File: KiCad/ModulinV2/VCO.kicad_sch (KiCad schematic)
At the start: 99 parts, among them Q1 MMBFJ201, Q2 MMBFJ201, SW3 SW_SPDT_MSM, U3 AS3340, U4 AS3340, U5 TL074HIDR, U6 TL074HIDR, U7 TL072HIDR

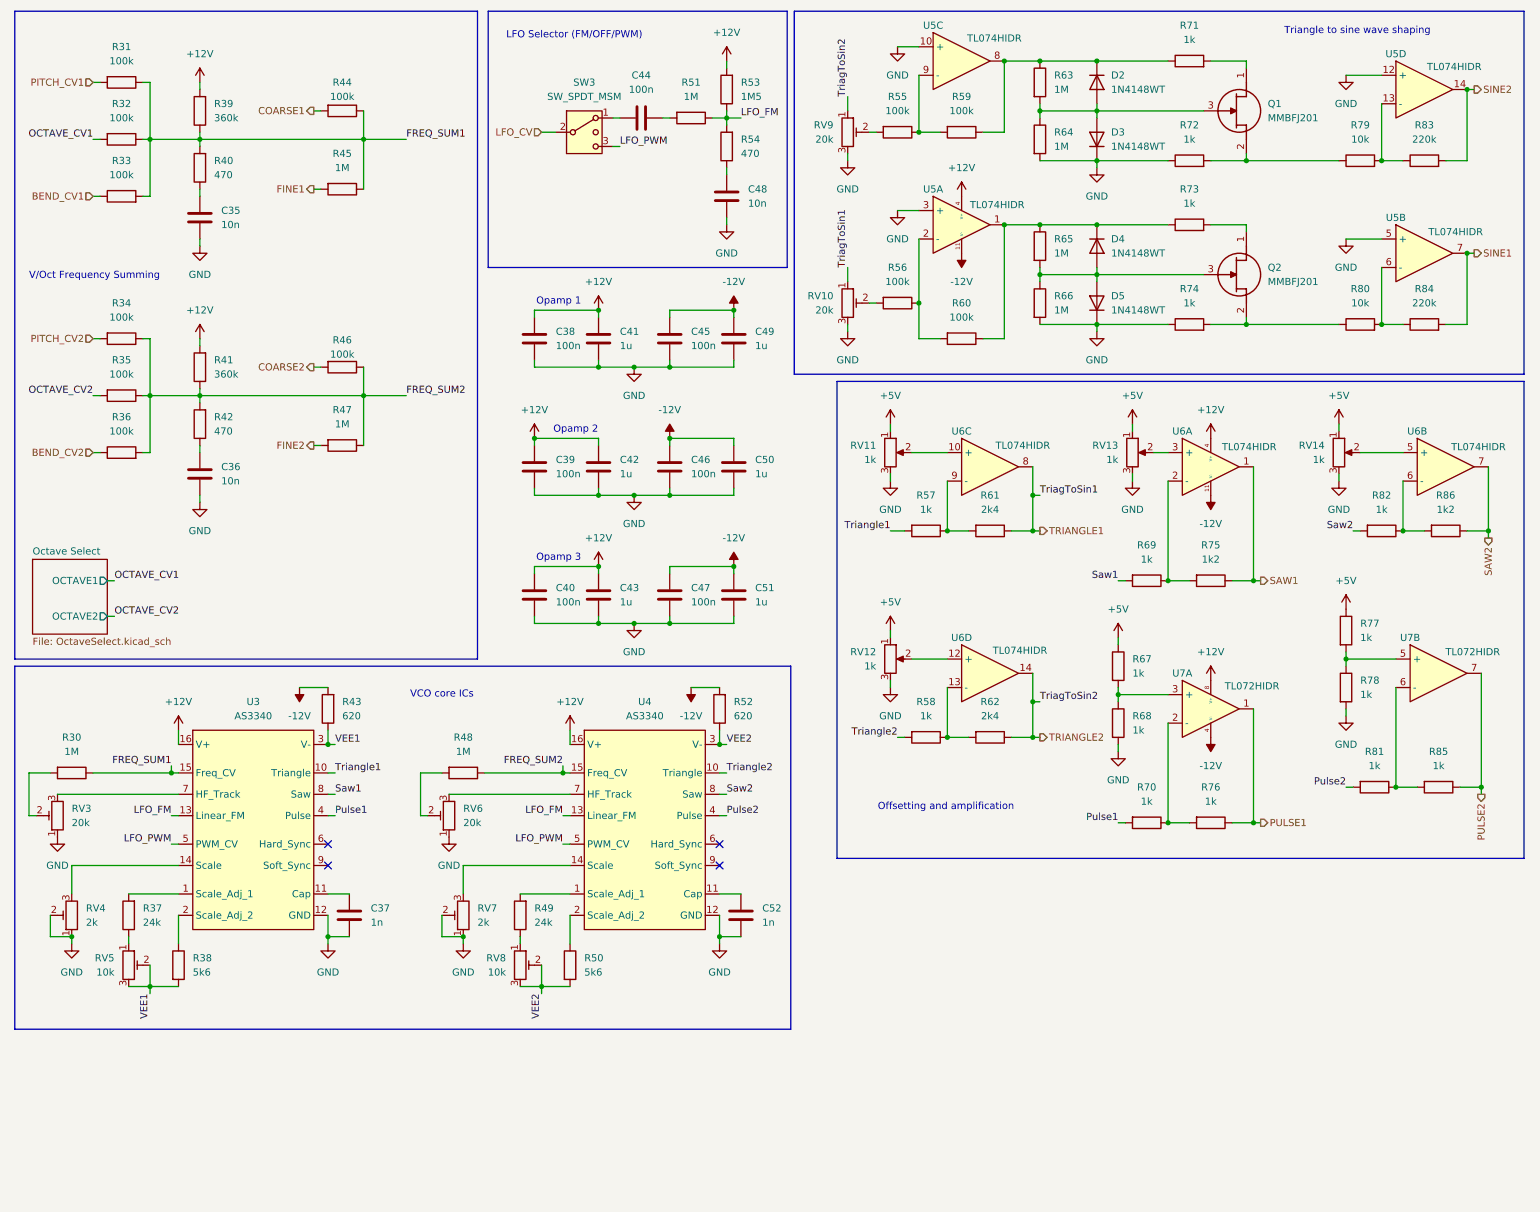
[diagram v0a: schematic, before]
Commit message: Fixed library issues and assigned most footprints
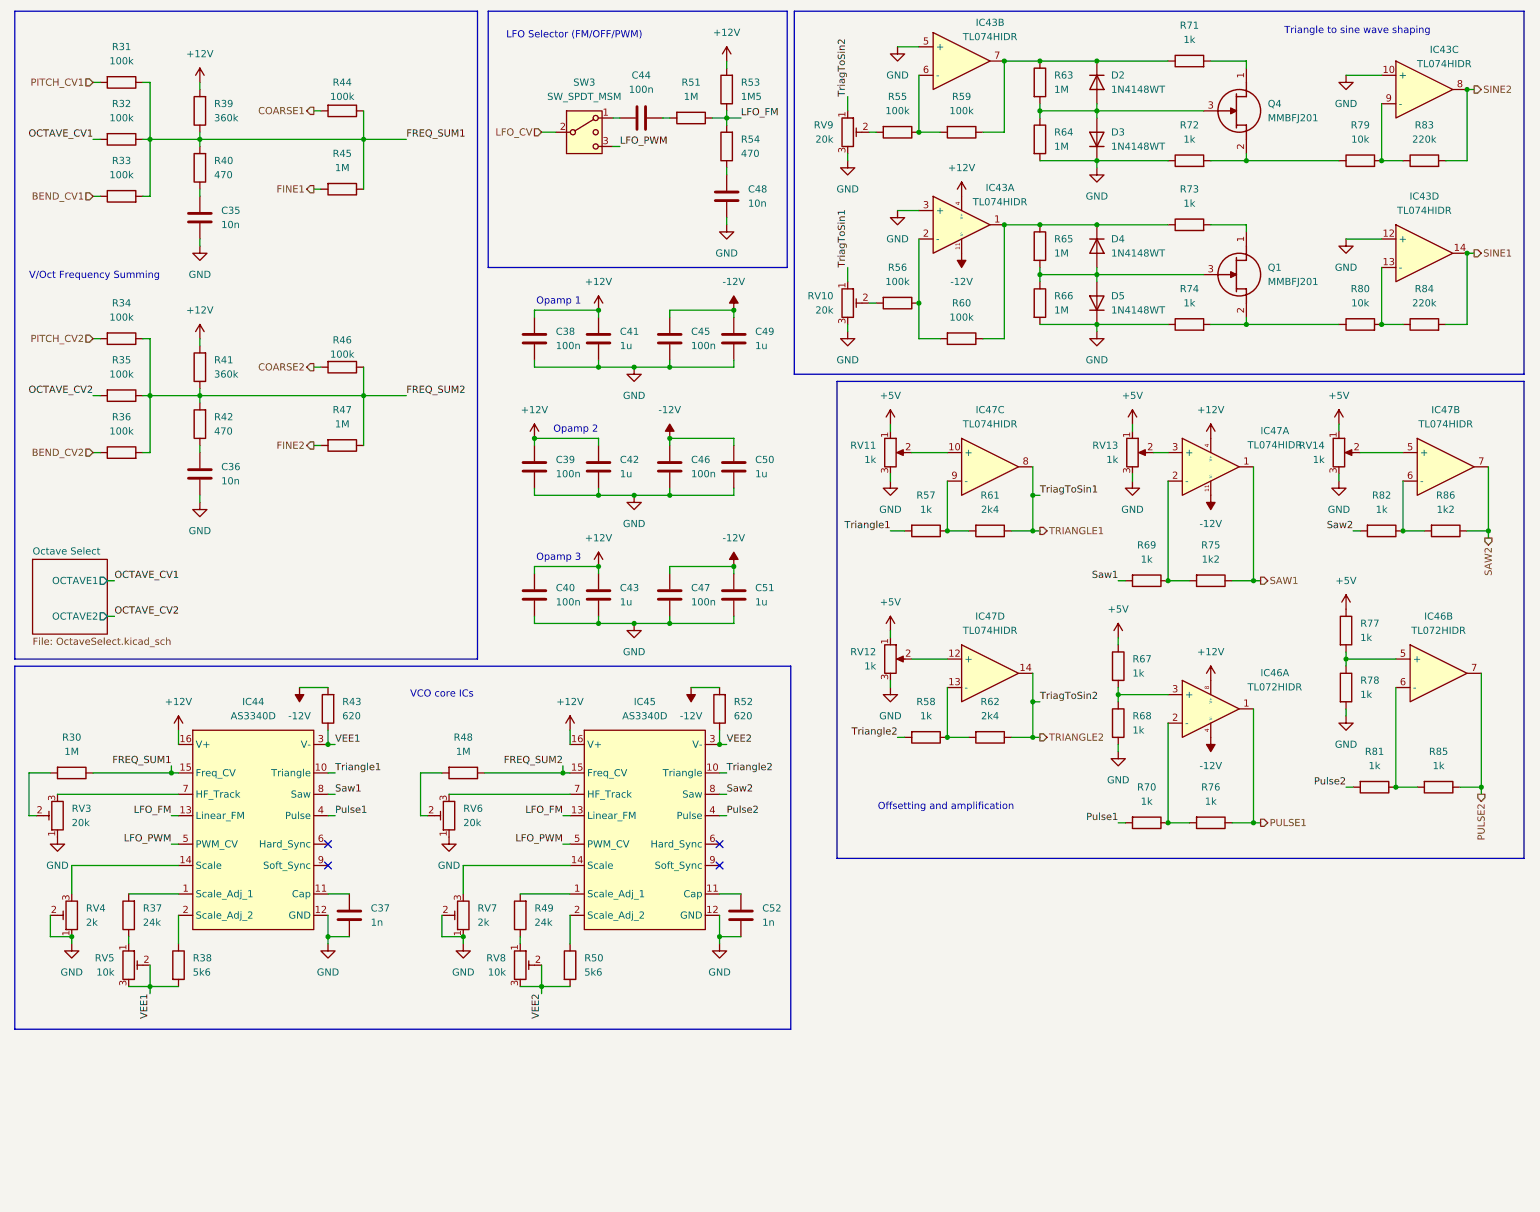
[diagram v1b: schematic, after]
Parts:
- removed Q1, Q2: MMBFJ201, SOT95P240X120-3N, symbol MMBFJ201:MMBFJ201
- removed U3, U4: AS3340, symbol AS3340:AS3340
- removed U5, U6: TL074HIDR, symbol TL074HIDR:TL074HIDRx4
- removed U7: TL072HIDR, symbol TL072HIDR:TL072HIDRx2
- added IC43, IC47: TL074HIDR, SamacSys_Parts:SOIC127P600X175-14N, symbol SamacSys_Parts:TL074HIDR
- added IC44, IC45: AS3340D, SamacSys_Parts:DIP762W46P254L2007H436Q16N, symbol SamacSys_Parts:AS3340D
- added IC46: TL072HIDR, SamacSys_Parts:SOIC127P600X175-8N, symbol SamacSys_Parts:TL072HIDR
- added Q1, Q4: MMBFJ201, SamacSys_Parts:SOT95P240X120-3N, symbol SamacSys_Parts:MMBFJ201
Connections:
- net +12V: now also IC43.4 (V+), IC44.16 (V+), IC45.16 (V+), IC46.8 (V+), IC47.4 (V+)
- net -12V: now also IC43.11 (V-), IC46.4 (V-), IC47.11 (V-)
- net FREQ_SUM1: now also IC44.15 (Freq_CV)
- net FREQ_SUM2: now also IC45.15 (Freq_CV)
- net GND: now also IC43.10 (+), IC43.12 (+), IC43.3 (+), IC43.5 (+), IC44.12 (GND), IC45.12 (GND)
- net LFO_FM: now also IC44.13 (Linear_FM), IC45.13 (Linear_FM)
- net LFO_PWM: now also IC44.5 (PWM_CV), IC45.5 (PWM_CV)
- net PULSE1: now also IC46.1
- net PULSE2: now also IC46.7
- net Pulse1: now also IC44.4 (Pulse)
- net Pulse2: now also IC45.4 (Pulse)
- net SAW1: now also IC47.1
- net SAW2: now also IC47.7
- net SINE1: now also IC43.14
- net SINE2: now also IC43.8
- net Saw1: now also IC44.8 (Saw)
- net Saw2: now also IC45.8 (Saw)
- net TRIANGLE1: now also IC47.8
- net TRIANGLE2: now also IC47.14
- net Triangle1: now also IC44.10 (Triangle)
- net Triangle2: now also IC45.10 (Triangle)
- net VEE1: now also IC44.3 (V-)
- net VEE2: now also IC45.3 (V-)
- net at RV14.2: now also IC47.5 (+)
- net at R82.1, R86.2: now also IC47.6 (-)
- net at R71.2: now also Q4.1 (D)
- net at R72.2, R79.1: now also Q4.2 (S)
- net at D2.2 (A), D3.2 (A), R63.2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: now also Q4.3 (G)
- net at D2.1 (K), R59.1, R63.1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: now also IC43.7
- net at C37.1: now also IC44.11 (Cap)
- net at R70.1, R76.2: now also IC46.2 (-)
- net at R67.2, R68.1: now also IC46.3 (+)
- net at RV11.2: now also IC47.10 (+)
- net at R57.1, R61.2: now also IC47.9 (-)
- net at D4.1 (K), R60.1, R65.1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: now also IC43.1
- net at R56.1, R60.2: now also IC43.2 (-)
- net at R79.2, R83.1: now also IC43.9 (-)
- net at R81.1, R85.2: now also IC46.6 (-)
- net at R37.2: now also IC44.1 (Scale_Adj_1)
- net at D4.2 (A), D5.2 (A), R65.2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: now also Q1.3 (G)
- net at RV3.3: now also IC44.7 (HF_Track)
- net at RV6.3: now also IC45.7 (HF_Track)
- net at R49.2: now also IC45.1 (Scale_Adj_1)
- net at C52.1: now also IC45.11 (Cap)
- net at RV7.3: now also IC45.14 (Scale)
- net at R50.1: now also IC45.2 (Scale_Adj_2)
- net at RV12.2: now also IC47.12 (+)
- net at R58.1, R62.2: now also IC47.13 (-)
- net at RV4.3: now also IC44.14 (Scale)
- net at R77.2, R78.1: now also IC46.5 (+)
- net at R74.2, R80.1: now also Q1.2 (S)
- net at R80.2, R84.1: now also IC43.13 (-)
- net at R38.1: now also IC44.2 (Scale_Adj_2)
- net at R69.1, R75.2: now also IC47.2 (-)
- net at RV13.2: now also IC47.3 (+)
- net at R55.1, R59.2: now also IC43.6 (-)
- net at R73.2: now also Q1.1 (D)

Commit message: Changed switch for the boot and nrst. Fixed the GATE interface trigger
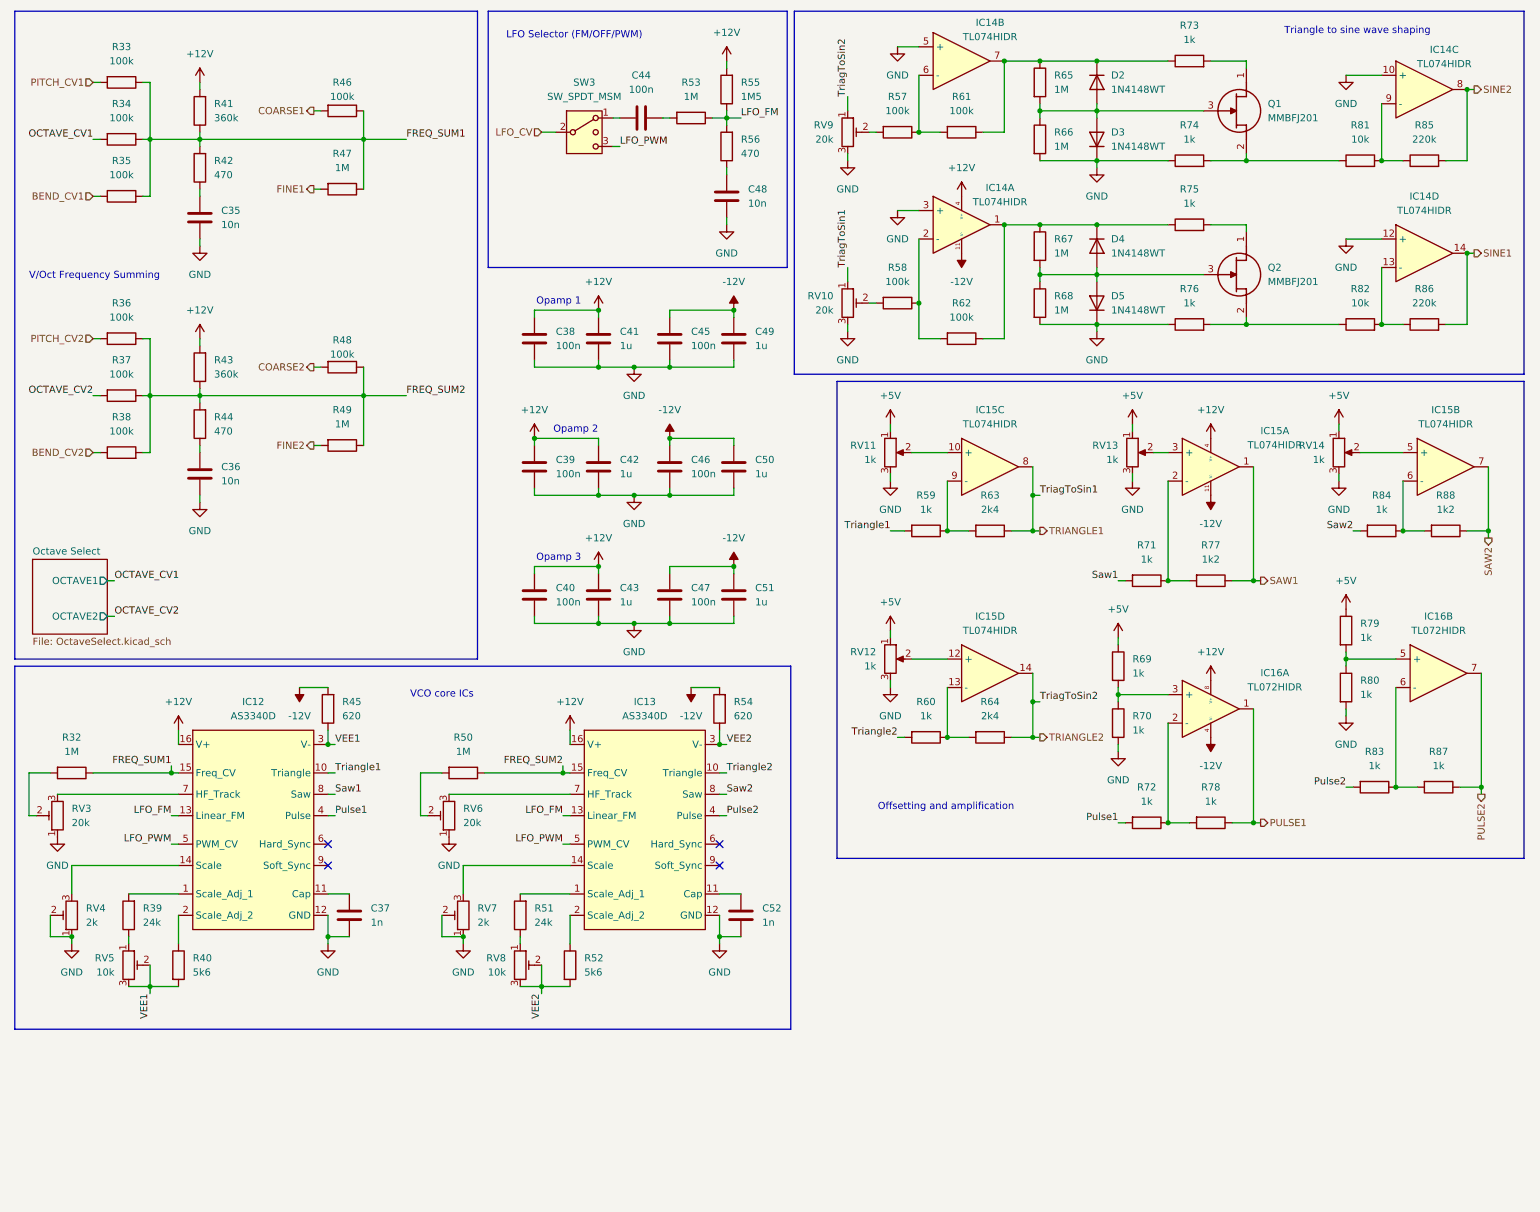
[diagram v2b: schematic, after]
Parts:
- renumbered IC44 to IC12, IC45 to IC13, IC43 to IC14, IC47 to IC15, IC46 to IC16, Q4 to Q1, Q1 to Q2, R30 to R32, R31 to R33, R32 to R34, R33 to R35, R34 to R36, R35 to R37, R36 to R38, R37 to R39, R38 to R40, R39 to R41, R40 to R42, R41 to R43, R42 to R44, R43 to R45, R44 to R46, R45 to R47, R46 to R48, R47 to R49, R48 to R50, R49 to R51, R50 to R52, R51 to R53, R52 to R54, R53 to R55, R54 to R56, R55 to R57, R56 to R58, R57 to R59, R58 to R60, R59 to R61, R60 to R62, R61 to R63, R62 to R64, R63 to R65, R64 to R66, R65 to R67, R66 to R68, R67 to R69, R68 to R70, R69 to R71, R70 to R72, R71 to R73, R72 to R74, R73 to R75, R74 to R76, R75 to R77, R76 to R78, R77 to R79, R78 to R80, R79 to R81, R80 to R82, R81 to R83, R82 to R84, R83 to R85, R84 to R86, R85 to R87, R86 to R88

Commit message: Started adding footprints for capacitors
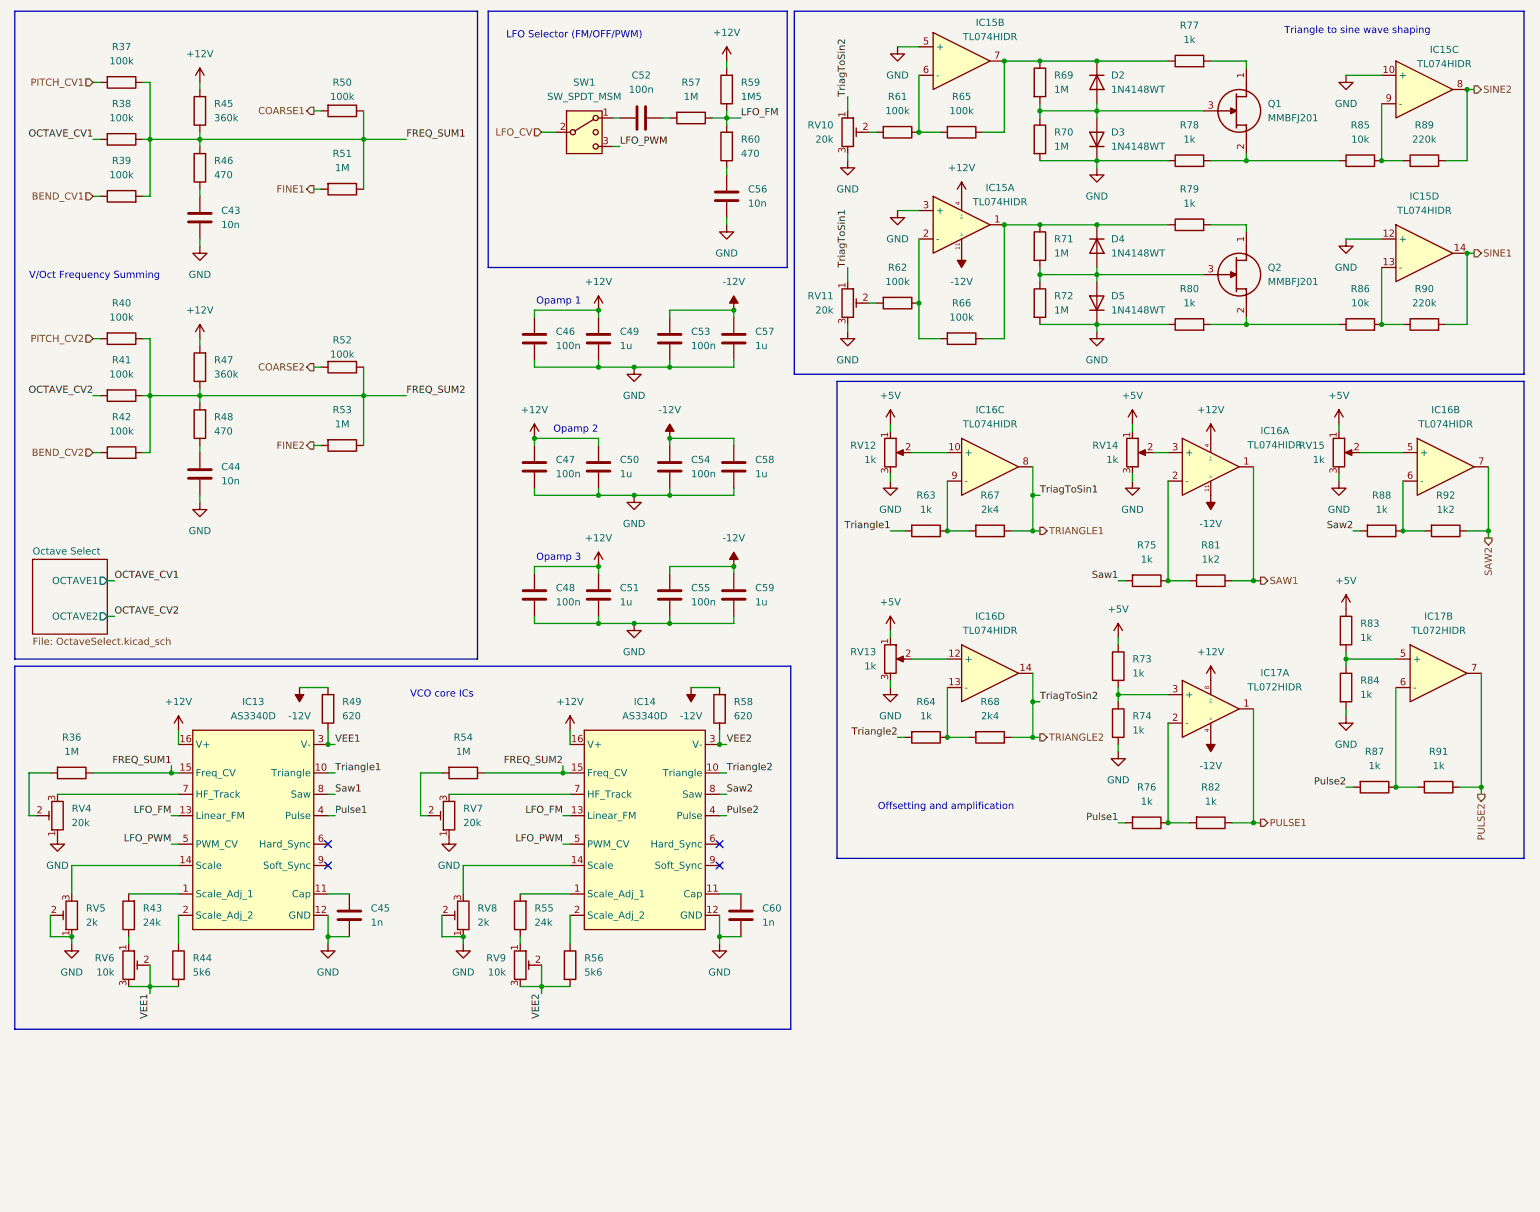
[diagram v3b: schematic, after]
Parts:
- C43: renamed from C35; footprint (none) -> SamacSys_Parts:CAPC1608X90N
- C44: renamed from C36; footprint (none) -> SamacSys_Parts:CAPC1608X90N
- C45: renamed from C37; footprint (none) -> SamacSys_Parts:CAPC1608X95N
- C46: renamed from C38; footprint (none) -> SamacSys_Parts:CAPC1608X90N
- C47: renamed from C39; footprint (none) -> SamacSys_Parts:CAPC1608X90N
- C48: renamed from C40; footprint (none) -> SamacSys_Parts:CAPC1608X90N
- C49: renamed from C41; footprint (none) -> SamacSys_Parts:CAPC1608X95N
- C50: renamed from C42; footprint (none) -> SamacSys_Parts:CAPC1608X95N
- C51: renamed from C43; footprint (none) -> SamacSys_Parts:CAPC1608X95N
- C52: renamed from C44; footprint (none) -> SamacSys_Parts:CAPC1608X90N
- C53: renamed from C45; footprint (none) -> SamacSys_Parts:CAPC1608X90N
- C54: renamed from C46; footprint (none) -> SamacSys_Parts:CAPC1608X90N
- C55: renamed from C47; footprint (none) -> SamacSys_Parts:CAPC1608X90N
- C56: renamed from C48; footprint (none) -> SamacSys_Parts:CAPC1608X90N
- C57: renamed from C49; footprint (none) -> SamacSys_Parts:CAPC1608X95N
- C58: renamed from C50; footprint (none) -> SamacSys_Parts:CAPC1608X95N
- C59: renamed from C51; footprint (none) -> SamacSys_Parts:CAPC1608X95N
- C60: renamed from C52; footprint (none) -> SamacSys_Parts:CAPC1608X95N
- SW1: renamed from SW3; footprint (none) -> SamacSys_Parts:SPDT
- renumbered IC12 to IC13, IC13 to IC14, IC14 to IC15, IC15 to IC16, IC16 to IC17, R32 to R36, R33 to R37, R34 to R38, R35 to R39, R36 to R40, R37 to R41, R38 to R42, R39 to R43, R40 to R44, R41 to R45, R42 to R46, R43 to R47, R44 to R48, R45 to R49, R46 to R50, R47 to R51, R48 to R52, R49 to R53, R50 to R54, R51 to R55, R52 to R56, R53 to R57, R54 to R58, R55 to R59, R56 to R60, R57 to R61, R58 to R62, R59 to R63, R60 to R64, R61 to R65, R62 to R66, R63 to R67, R64 to R68, R65 to R69, R66 to R70, R67 to R71, R68 to R72, R69 to R73, R70 to R74, R71 to R75, R72 to R76, R73 to R77, R74 to R78, R75 to R79, R76 to R80, R77 to R81, R78 to R82, R79 to R83, R80 to R84, R81 to R85, R82 to R86, R83 to R87, R84 to R88, R85 to R89, R86 to R90, R87 to R91, R88 to R92, RV9 to RV10, RV10 to RV11, RV11 to RV12, RV12 to RV13, RV13 to RV14, RV14 to RV15, RV3 to RV4, RV4 to RV5, RV5 to RV6, RV6 to RV7, RV7 to RV8, RV8 to RV9
